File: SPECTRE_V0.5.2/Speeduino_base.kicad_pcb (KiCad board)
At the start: 2 copper layers, 100 x 93 mm, 211 parts, among them J1 Conn_01x06_Male, J2 Conn_02x04_Odd_Even, J3 ProtoArea, Q1 AO3400, Q10 BSP78, Q11 BSP78, Q12 AO3400, Q13 BSP78, Q14 BSP78, Q15 BSP78, Q16 BSP78, Q17 BSP78, Q18 BSP78, Q19 BSP78, Q20 BSP78, Q21 BSP78, Q6 AO3400, Q7 AO3400, U1 MAX9926UAEE+, U10 MIC4427, U2 LM78M05_TO220, U3 TL431DBZ, U4 molex_48pin, U5 TJA1050, U6 MAX3232, U7 MIC4427, U8 MIC4427, U9 MIC4427

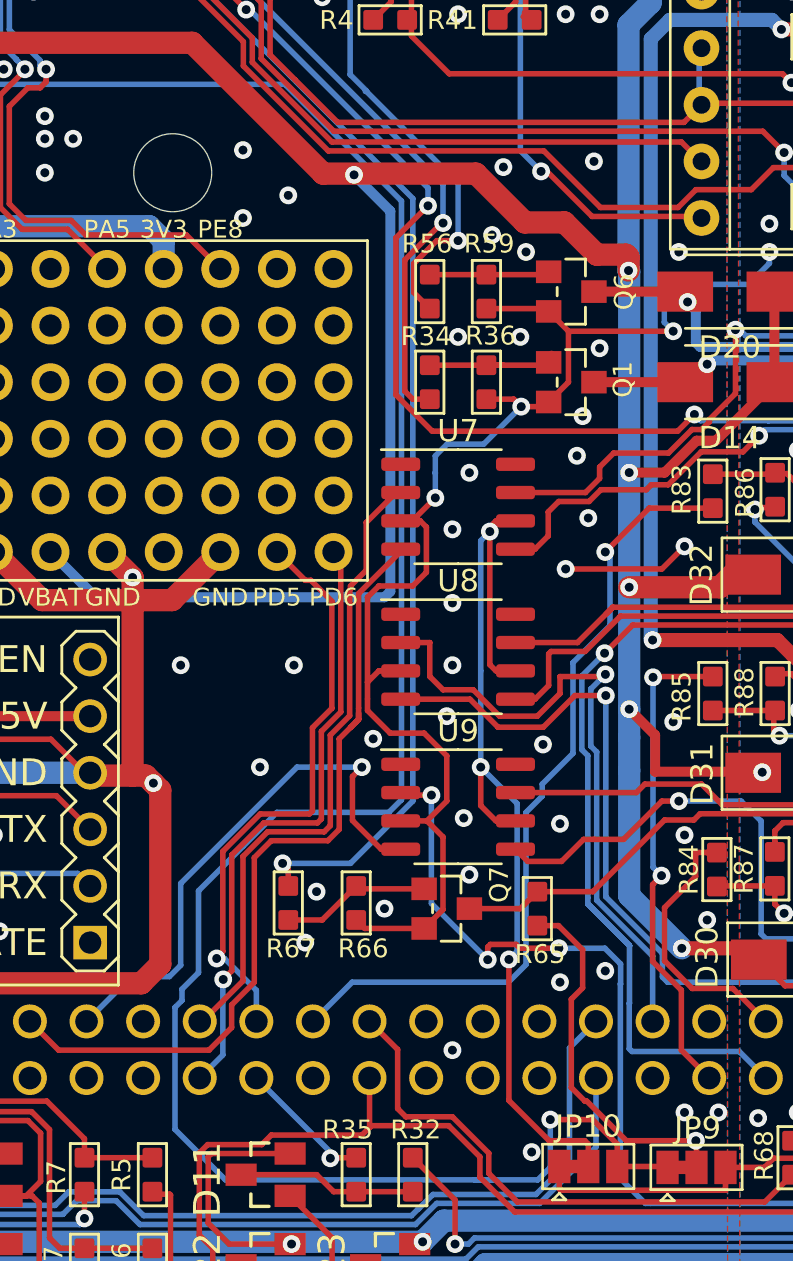
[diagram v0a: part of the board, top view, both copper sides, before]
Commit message: update molex 48 pin to correct location
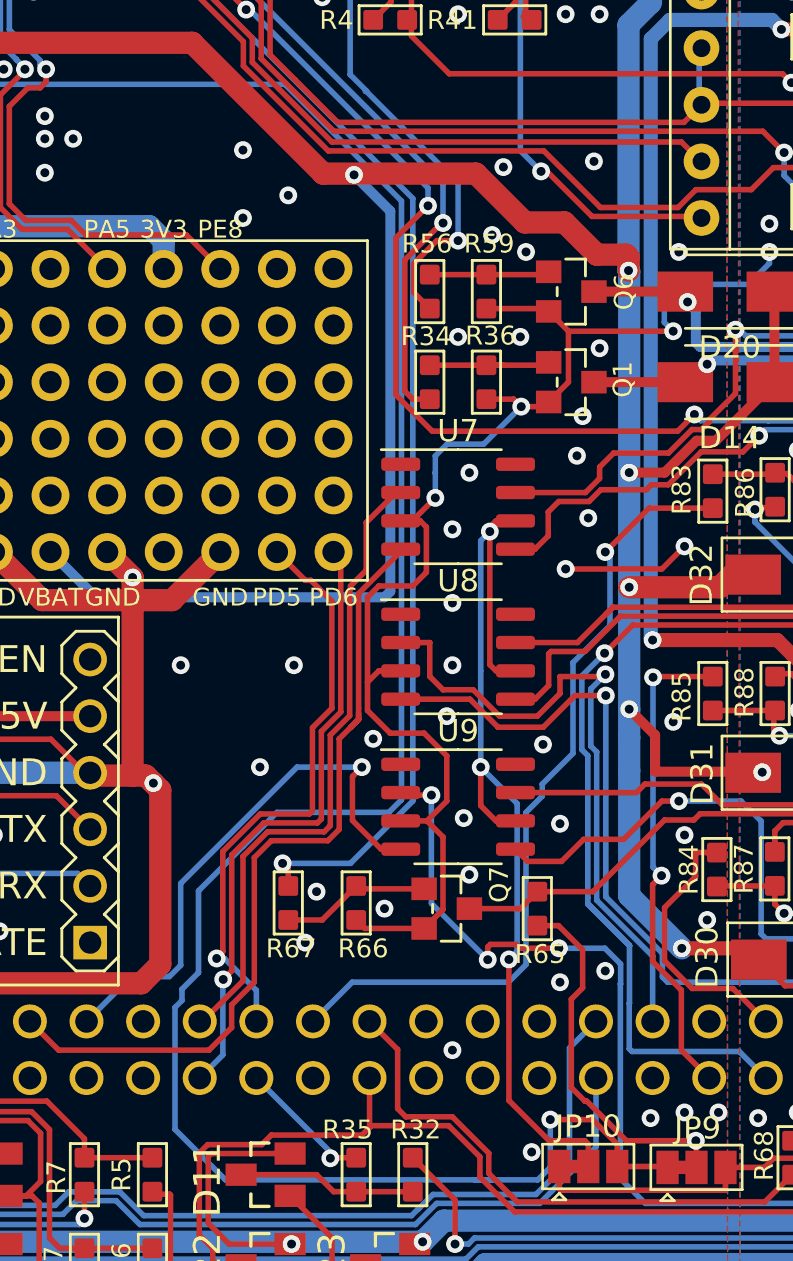
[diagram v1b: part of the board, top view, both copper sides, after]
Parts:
- U2: footprint Package_TO_SOT_THT:TO-220-3_Horizontal_TabUp -> Package_TO_SOT_THT:TO-220-3_Vertical
- U4: footprint rusefi_lib:Molex_48 -> Speeduino_base:Molex_48
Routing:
- net (no net): vias 0 -> 1
